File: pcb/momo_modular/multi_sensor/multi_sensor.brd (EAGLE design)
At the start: 100 x 33 mm, 38 parts, among them U1 MCP6001U, U10 SM5470-DIFF-PRESS-SENSOR, U11 TCR2EF28-LINREG, U2 16LF1847, U3 DUAL-BUFFER-OD-NC7WZ07, U4 LT1990, U5 2:1-MUX, U6 2:1-MUX, U7 AD8557-DIGITRIM-OPAMP, U8 2:1-MUX, U9 2:1-MUX

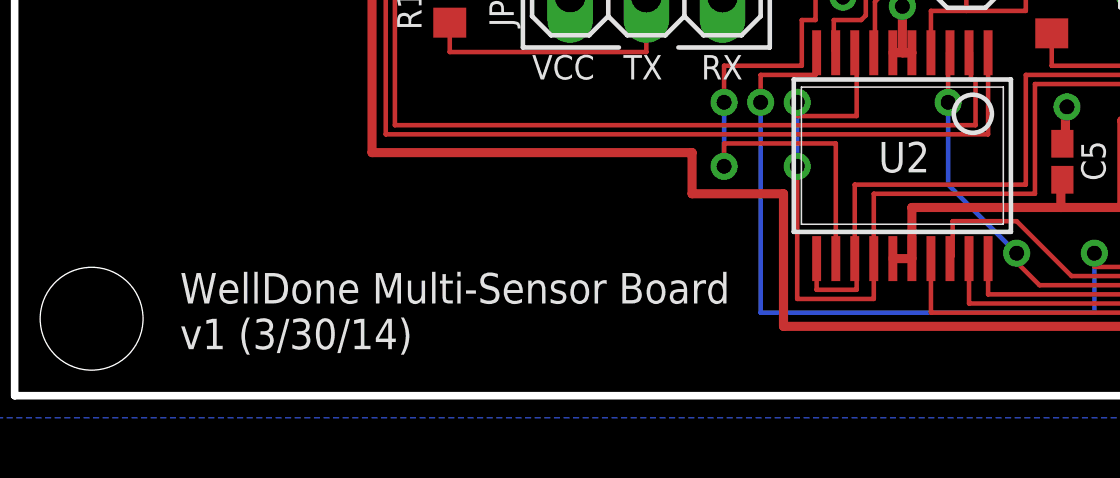
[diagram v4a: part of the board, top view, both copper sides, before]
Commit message: Update version numbers
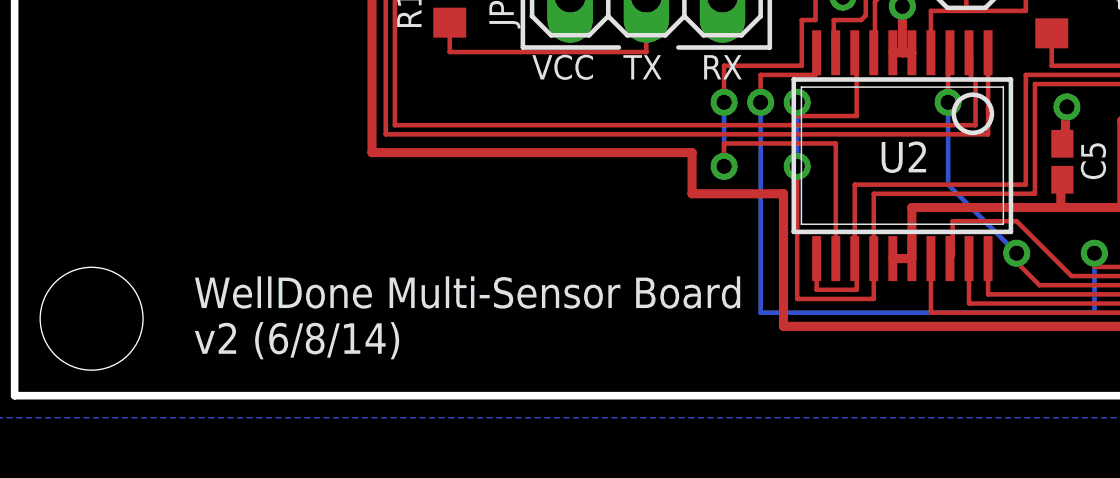
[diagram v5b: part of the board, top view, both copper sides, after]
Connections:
- removed net V3_IN: JP8.1
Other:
- board text added: "WellDone Multi-Sensor Board v2 (6/8/14)"
- board text removed: "WellDone Multi-Sensor Board v1 (3/30/14)"
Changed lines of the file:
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@@
 <text x="46.7868" y="7.1628" size="0.8128" layer="21">VCC</text>
 <text x="49.3776" y="26.9748" size="1.016" layer="21">Pressure Sensor</text>
-<text x="9.2964" y="5.334" size="1.016" layer="21">WellDone Multi-Sensor Board
-v1 (3/30/14)</text>
+<text x="9.7536" y="5.1816" size="1.016" layer="21">WellDone Multi-Sensor Board
+v2 (6/8/14)</text>
 <text x="81.9912" y="16.9164" size="1.016" layer="21" rot="R180">Current
 Sensor</text>
@@
 <wire x1="98.6028" y1="22.186" x2="99.6696" y2="22.186" width="0.1524" layer="1"/>
 </signal>
-<signal name="V3_IN">
-<contactref element="JP8" pad="1"/>
-</signal>
 <signal name="N$3">
